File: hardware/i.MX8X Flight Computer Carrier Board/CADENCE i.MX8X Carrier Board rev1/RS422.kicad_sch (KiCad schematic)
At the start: 9 parts, among them CN1 DF11-16DP-2DSA(08), U18 MAX3485, U19 SN65C1168ERGYR

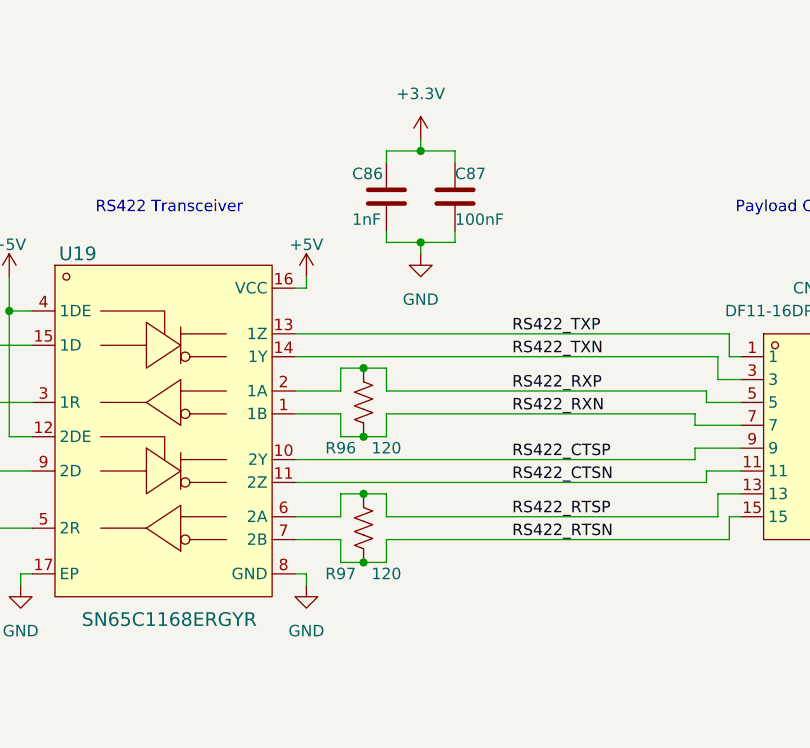
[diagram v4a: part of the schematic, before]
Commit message: cchanges after phytec review
- fixed issue with ospi chip select line & clk line
- replaced 1k pulldowns with 10k pulldowns and added 1k series resistors to 1.8V line for boot config lines
-removed unused global label tags from som and changed to nc
- repinmuxed for potential watchdog and ospi changes

to do:
-microSD
-reallocate gpios (extras to breakout)
-create 8pin jst connector for lucid camera (12V pwr)
- give satnogs additional uart
- reorg/rename global labels
-watchdog input pin reassign to c62 potentially after feedback from max
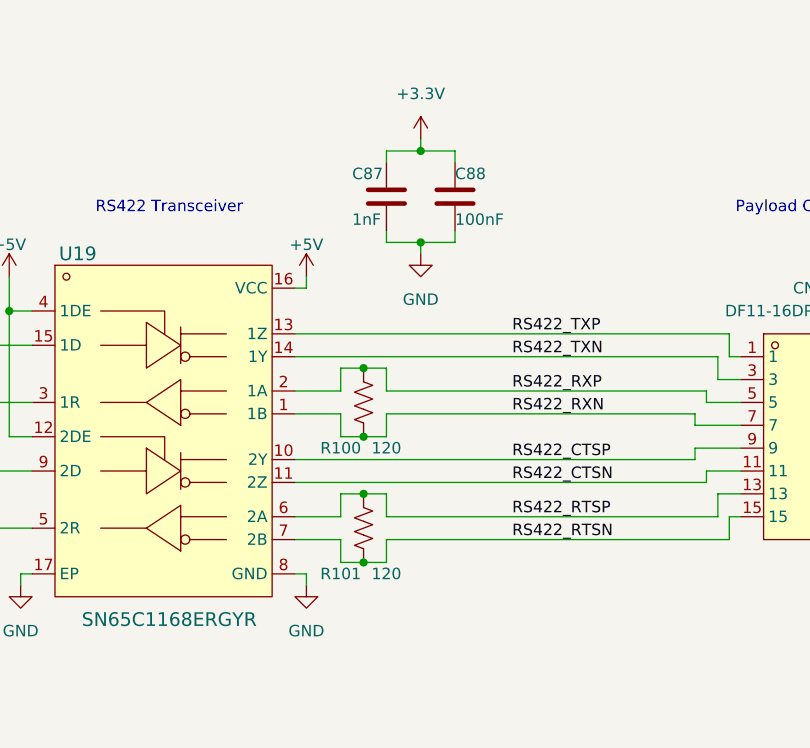
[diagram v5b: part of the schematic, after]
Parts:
- renumbered C86 to C87, C87 to C88, R96 to R100, R97 to R101
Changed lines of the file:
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@@
 		(on_board yes)
 		(dnp no)
-		(property "Reference" "R97"
+		(property "Reference" "R101"
 			(at 113.03 88.9 0)
 			(effects
@@
 			(project "CADENCE i.MX8X Carrier Board rev1"
 				(path "/de284495-d382-47cb-b528-76e440980d40/c0bf5d3f-4cfb-4c0b-b448-903517df1d5a"
-					(reference "R97")
+					(reference "R101")
 					(unit 1)
 				)
@@
 		(dnp no)
 		(fields_autoplaced yes)
-		(property "Reference" "#PWR0117"
+		(property "Reference" "#PWR0118"
 			(at 109.22 96.52 0)
 			(effects
@@
 			(project "CADENCE i.MX8X Carrier Board rev1"
 				(path "/de284495-d382-47cb-b528-76e440980d40/c0bf5d3f-4cfb-4c0b-b448-903517df1d5a"
-					(reference "#PWR0117")
+					(reference "#PWR0118")
 					(unit 1)
 				)
@@
 		(on_board yes)
 		(dnp no)
-		(property "Reference" "R96"
+		(property "Reference" "R100"
 			(at 113.03 74.93 0)
 			(effects
@@
 			(project "CADENCE i.MX8X Carrier Board rev1"
 				(path "/de284495-d382-47cb-b528-76e440980d40/c0bf5d3f-4cfb-4c0b-b448-903517df1d5a"
-					(reference "R96")
+					(reference "R100")
 					(unit 1)
 				)
@@
 		(on_board yes)
 		(dnp no)
-		(property "Reference" "C86"
+		(property "Reference" "C87"
 			(at 114.3 44.45 0)
 			(effects
@@
 			(project "CADENCE i.MX8X Carrier Board rev1"
 				(path "/de284495-d382-47cb-b528-76e440980d40/c0bf5d3f-4cfb-4c0b-b448-903517df1d5a"
-					(reference "C86")
+					(reference "C87")
 					(unit 1)
 				)
@@
 		(on_board yes)
 		(dnp no)
-		(property "Reference" "C87"
+		(property "Reference" "C88"
 			(at 125.73 44.45 0)
 			(effects
@@
 			(project "CADENCE i.MX8X Carrier Board rev1"
 				(path "/de284495-d382-47cb-b528-76e440980d40/c0bf5d3f-4cfb-4c0b-b448-903517df1d5a"
-					(reference "C87")
+					(reference "C88")
 					(unit 1)
 				)
@@
 		(dnp no)
 		(fields_autoplaced yes)
-		(property "Reference" "#PWR0112"
+		(property "Reference" "#PWR0113"
 			(at -191.77 102.87 0)
 			(effects
@@
 			(project "CADENCE i.MX8X Carrier Board rev1"
 				(path "/de284495-d382-47cb-b528-76e440980d40/c0bf5d3f-4cfb-4c0b-b448-903517df1d5a"
-					(reference "#PWR0112")
+					(reference "#PWR0113")
 					(unit 1)
 				)
@@
 		(dnp no)
 		(fields_autoplaced yes)
-		(property "Reference" "#PWR0118"
+		(property "Reference" "#PWR0119"
 			(at 121.92 44.45 0)
 			(effects
@@
 			(project "CADENCE i.MX8X Carrier Board rev1"
 				(path "/de284495-d382-47cb-b528-76e440980d40/c0bf5d3f-4cfb-4c0b-b448-903517df1d5a"
-					(reference "#PWR0118")
+					(reference "#PWR0119")
 					(unit 1)
 				)
@@
 		(dnp no)
 		(fields_autoplaced yes)
-		(property "Reference" "#PWR0120"
+		(property "Reference" "#PWR0121"
 			(at 173.99 91.44 0)
 			(effects
@@
 			(project "CADENCE i.MX8X Carrier Board rev1"
 				(path "/de284495-d382-47cb-b528-76e440980d40/c0bf5d3f-4cfb-4c0b-b448-903517df1d5a"
-					(reference "#PWR0120")
+					(reference "#PWR0121")
 					(unit 1)
 				)
@@
 		(on_board yes)
 		(dnp no)
-		(property "Reference" "#PWR0113"
+		(property "Reference" "#PWR0114"
 			(at -191.77 139.7 0)
 			(effects
@@
 			(project "CADENCE i.MX8X Carrier Board rev1"
 				(path "/de284495-d382-47cb-b528-76e440980d40/c0bf5d3f-4cfb-4c0b-b448-903517df1d5a"
-					(reference "#PWR0113")
+					(reference "#PWR0114")
 					(unit 1)
 				)
@@
 		(on_board yes)
 		(dnp no)
-		(property "Reference" "#PWR0114"
+		(property "Reference" "#PWR0115"
 			(at 76.2 59.69 0)
 			(effects
@@
 			(project "CADENCE i.MX8X Carrier Board rev1"
 				(path "/de284495-d382-47cb-b528-76e440980d40/c0bf5d3f-4cfb-4c0b-b448-903517df1d5a"
-					(reference "#PWR0114")
+					(reference "#PWR0115")
 					(unit 1)
 				)
@@
 		(dnp no)
 		(fields_autoplaced yes)
-		(property "Reference" "#PWR0115"
+		(property "Reference" "#PWR0116"
 			(at 77.47 96.52 0)
 			(effects
@@
 			(project "CADENCE i.MX8X Carrier Board rev1"
 				(path "/de284495-d382-47cb-b528-76e440980d40/c0bf5d3f-4cfb-4c0b-b448-903517df1d5a"
-					(reference "#PWR0115")
+					(reference "#PWR0116")
 					(unit 1)
 				)
@@
 		(on_board yes)
 		(dnp no)
-		(property "Reference" "#PWR0116"
+		(property "Reference" "#PWR0117"
 			(at 109.22 59.69 0)
 			(effects
@@
 			(project "CADENCE i.MX8X Carrier Board rev1"
 				(path "/de284495-d382-47cb-b528-76e440980d40/c0bf5d3f-4cfb-4c0b-b448-903517df1d5a"
-					(reference "#PWR0116")
+					(reference "#PWR0117")
 					(unit 1)
 				)
@@
 		(dnp no)
 		(fields_autoplaced yes)
-		(property "Reference" "#PWR0119"
+		(property "Reference" "#PWR0120"
 			(at 121.92 59.69 0)
 			(effects
@@
 			(project "CADENCE i.MX8X Carrier Board rev1"
 				(path "/de284495-d382-47cb-b528-76e440980d40/c0bf5d3f-4cfb-4c0b-b448-903517df1d5a"
-					(reference "#PWR0119")
-					(unit 1)
-				)
+					(reference "#PWR0120")
+					(unit 1)
+				)

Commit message: Finished footprints- Double check usbs
Only thing i didn't touch was watchdogs. That might still need to be changed.
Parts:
- C87, C88: footprint Capacitor_SMD:C_0603_1608Metric -> Capacitor_SMD:C_0402_1005Metric
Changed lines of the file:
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@@
 			)
 		)
-		(property "Footprint" "Capacitor_SMD:C_0603_1608Metric"
+		(property "Footprint" "Capacitor_SMD:C_0402_1005Metric"
 			(at 119.0752 50.8 0)
 			(effects
@@
 			)
 		)
-		(property "Footprint" "Capacitor_SMD:C_0603_1608Metric"
+		(property "Footprint" "Capacitor_SMD:C_0402_1005Metric"
 			(at 126.6952 50.8 0)
 			(effects

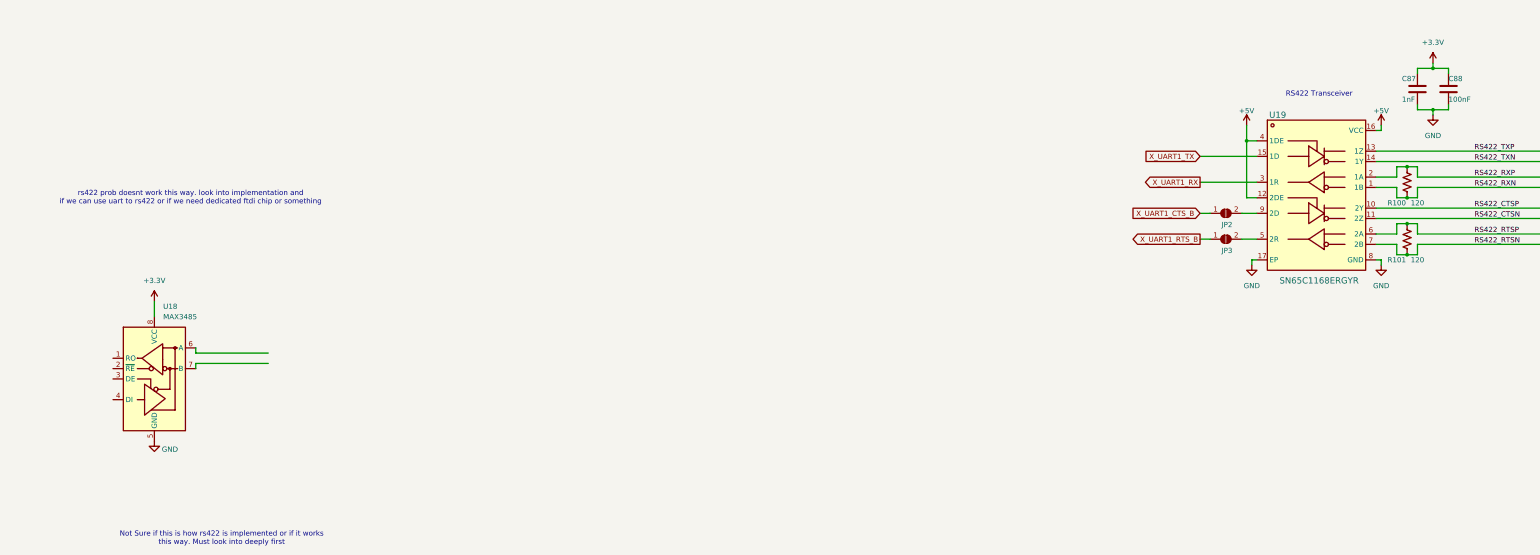
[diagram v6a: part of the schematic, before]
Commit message: Some ERC fixes, schematic annotations, pinmux for uSD & GPIO fixes, GPIO level shifter, footprint selection & pathway fix
component footprints for most part have been selected
going to double check again tmr
imx8x som bth samtec connector footprint needs to be adjusted as reference footprint uses each connector as individual symbol, while we have as part of one symbol (spacing between connector is important so som can fit in)
also one component didnt have part (uart mux) and havent assigned
implemented can bus interface with satnogs, moved around gpios, level shifted 8 gpios, fixed few missing connections (gps 1pps, a load switch enable gpio), resolved some erc errors/ symbol shorts, incorrect pinmux implementation around A9&10 for uSD and gpio, reannotated schematic, fixed footprint reference paths
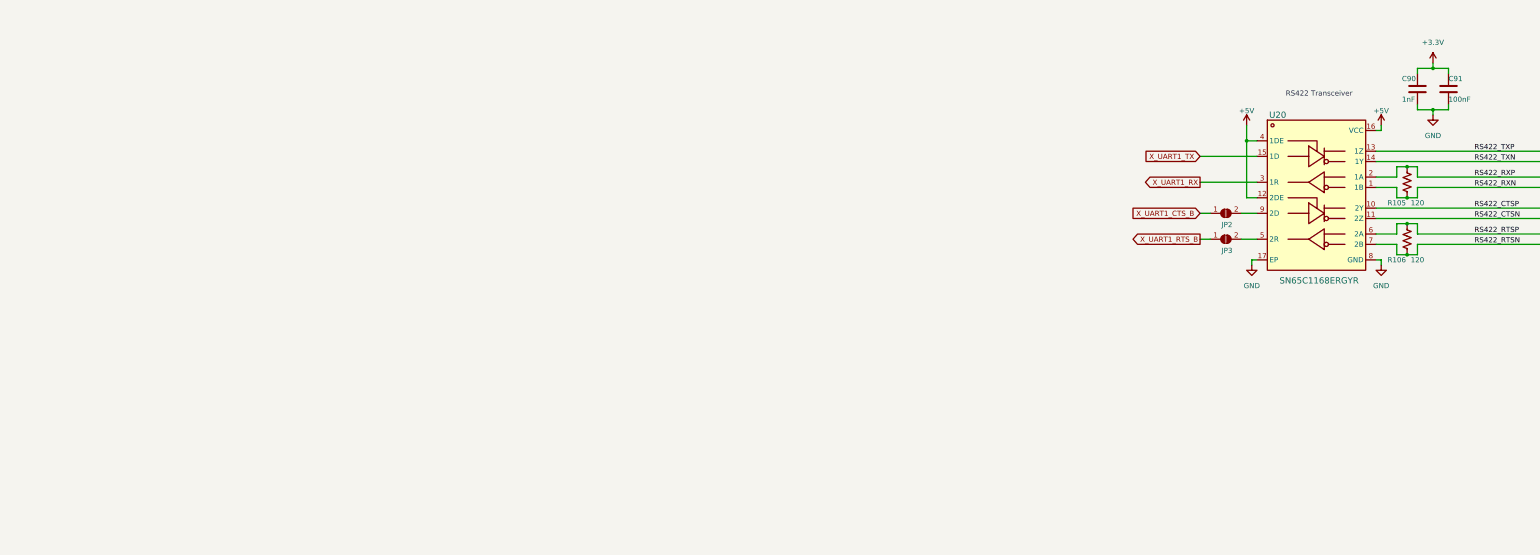
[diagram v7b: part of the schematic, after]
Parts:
- removed U18: MAX3485, Package_SO:SOIC-8_3.9x4.9mm_P1.27mm, symbol Interface_UART:MAX3485
- U20: renamed from U19; footprint easyeda2kicad:VQFN-16_L4.0-W3.5-P0.50-BL-EP -> SN65C1168ERGYR:RGY16_2P55X2P05
- renumbered C87 to C90, C88 to C91, R100 to R105, R101 to R106
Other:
- note removed: "Not Sure if this is how rs422 is implemented or if it works this way. Must look into deeply first"
- note removed: "rs422 prob doesnt work this way. look into implementation and if we can use uart to rs422 or if we need dedicated ftdi chip or something"

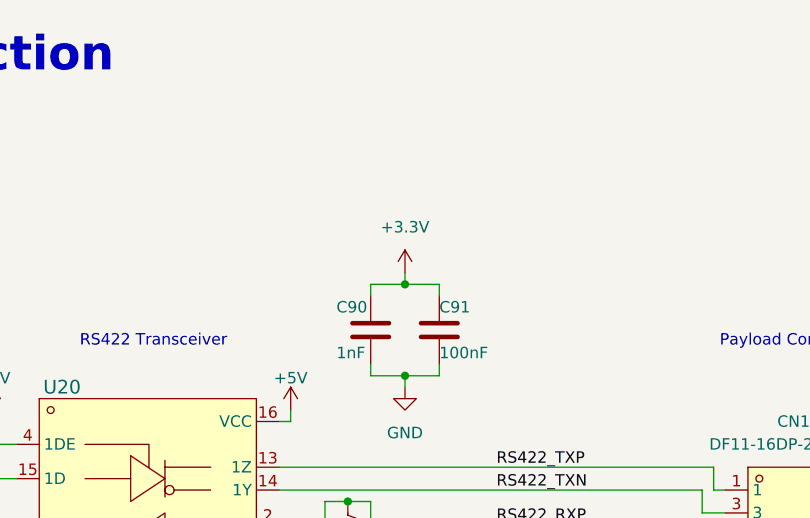
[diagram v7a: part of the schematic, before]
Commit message: preliminary pcb layout/parts placement on board
- finished imx8x som footprint
- adjusted a few footprints as well
- noticed usb-a footprint pad reference needs to be adjusted (will do later)
- preliminary edge cuts
- will need to add mounting holes
- changed rs422 page decoupling capacitor power net from 3.3v to 5v
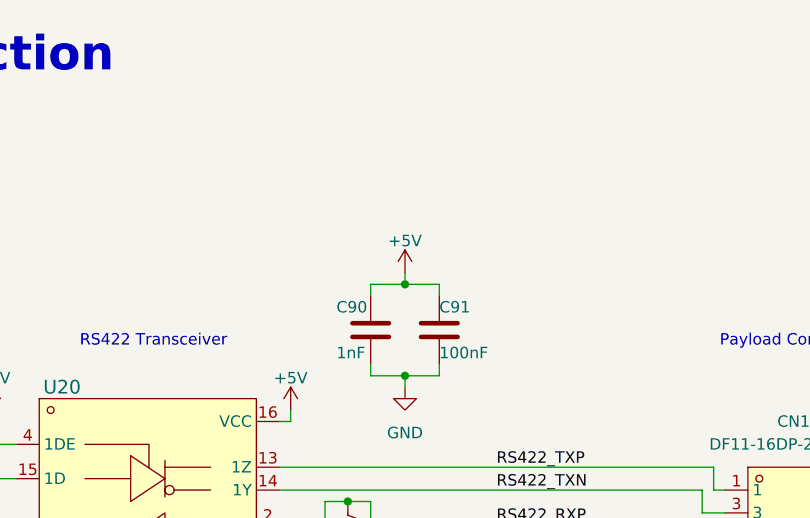
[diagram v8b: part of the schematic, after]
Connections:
- net +3.3V is gone; now on net +5V: C90.1, C91.1
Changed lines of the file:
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@@
 	)
 	(symbol
-		(lib_id "power:+3.3V")
+		(lib_id "power:+5V")
 		(at 121.92 40.64 0)
 		(unit 1)
@@
 		(on_board yes)
 		(dnp no)
-		(fields_autoplaced yes)
 		(property "Reference" "#PWR0122"
 			(at 121.92 44.45 0)
@@
 			)
 		)
-		(property "Value" "+3.3V"
-			(at 121.92 35.56 0)
+		(property "Value" "+5V"
+			(at 121.92 37.084 0)
 			(effects
 				(font
@@
 			)
 		)
-		(property "Description" "Power symbol creates a global label with name \"+3.3V\""
+		(property "Description" "Power symbol creates a global label with name \"+5V\""
 			(at 121.92 40.64 0)
 			(effects
